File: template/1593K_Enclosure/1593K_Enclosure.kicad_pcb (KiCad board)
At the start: 2 copper layers, 56.6 x 57.7 mm, 1 part

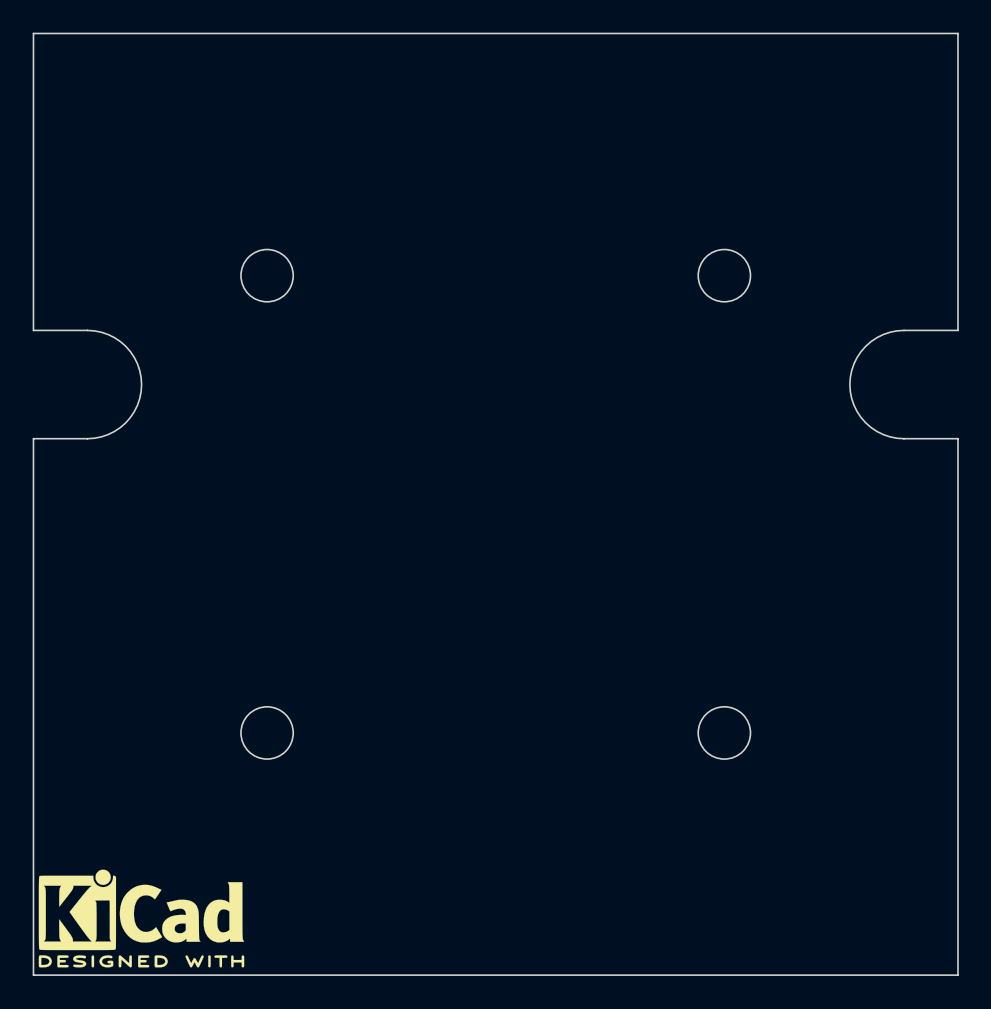
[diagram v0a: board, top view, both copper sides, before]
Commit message: Updated mounting holes from circular edge cuts to actual mounting holes. Added mounting hole symbols to schematic.
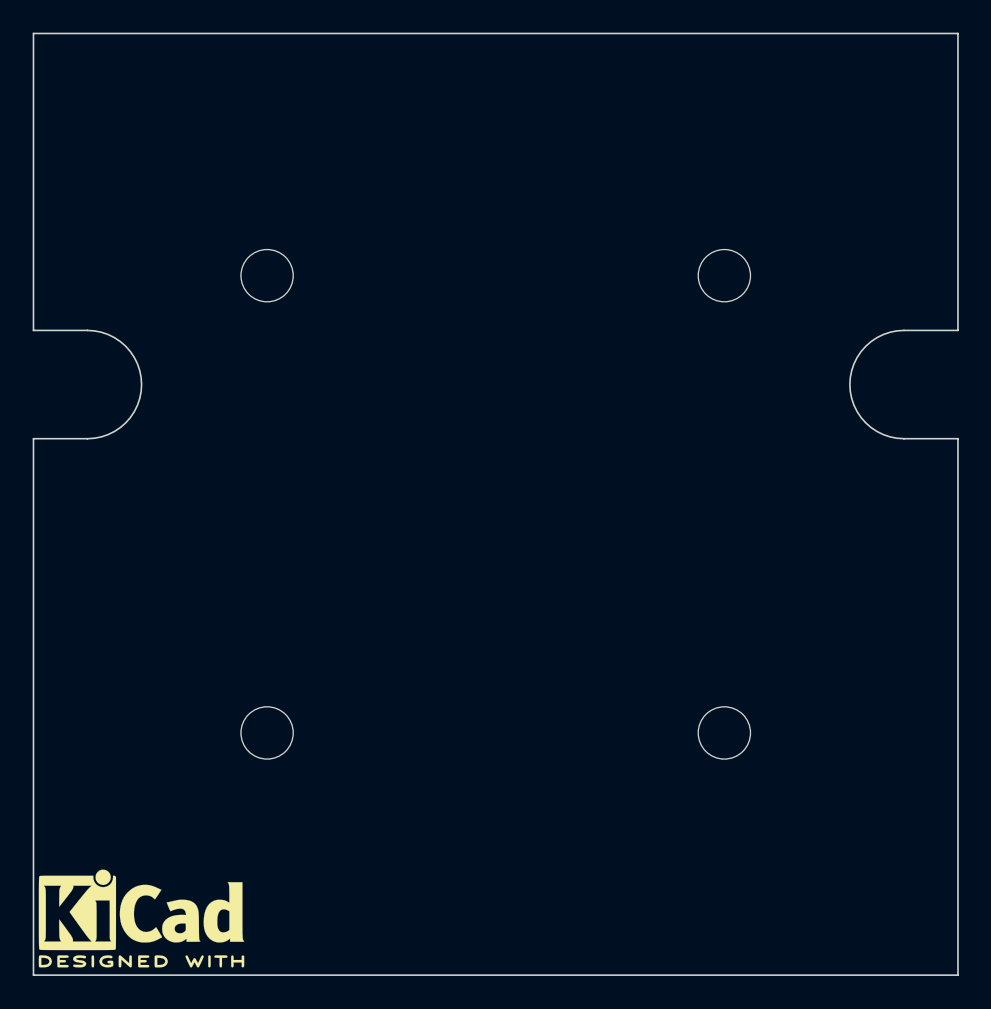
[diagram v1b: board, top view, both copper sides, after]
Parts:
- added MK1: MountingHole_3.2mm_M3_ISO14580, Mounting_Holes:MountingHole_3.2mm_M3_ISO14580, F.Cu at (87.7, 96.6)
- added MK2: MountingHole_3.2mm_M3_ISO14580, Mounting_Holes:MountingHole_3.2mm_M3_ISO14580, F.Cu at (115.7, 96.6)
- added MK3: MountingHole_3.2mm_M3_ISO14580, Mounting_Holes:MountingHole_3.2mm_M3_ISO14580, F.Cu at (87.7, 124.6)
- added MK4: MountingHole_3.2mm_M3_ISO14580, Mounting_Holes:MountingHole_3.2mm_M3_ISO14580, F.Cu at (115.7, 124.6)
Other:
- outline, holes or cut-outs redrawn
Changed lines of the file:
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@@
-(kicad_pcb (version 20160815) (host pcbnew no-vcs-found-undefined)
+(kicad_pcb (version 20160815) (host pcbnew no-vcs-found-7409~56~ubuntu16.10.1)
   (general
     (links 0)
@@
     (area 69.845 81.766999 134.395 145.67)
     (thickness 1.6)
-    (drawings 19)
+    (drawings 15)
     (tracks 0)
     (zones 0)
-    (modules 1)
+    (modules 5)
     (nets 1)
   )
@@
     (mod_text_size 1 1)
     (mod_text_width 0.15)
-    (pad_size 1.524 1.524)
-    (pad_drill 0.762)
+    (pad_size 3.2 3.2)
+    (pad_drill 3.2)
     (pad_to_mask_clearance 0.0762)
     (aux_axis_origin 130 100)
@@
     (diff_pair_width 0.2)
   )
+  (module Mounting_Holes:MountingHole_3.2mm_M3_ISO14580 locked (layer F.Cu)
+    (at 115.695 124.647)
+    (descr "Mounting Hole 3.2mm, no annular, M3, ISO14580")
+    (tags "mounting hole 3.2mm no annular m3 iso14580")
+    (fp_text reference MK4 (at 0 -3.75) (layer F.SilkS) hide
+      (effects (font (size 1 1) (thickness 0.15)))
+    )
+    (fp_text value MountingHole_3.2mm_M3_ISO14580 (at 0 3.75) (layer F.Fab) hide
+      (effects (font (size 1 1) (thickness 0.15)))
+    )
+    (fp_circle (center 0 0) (end 3 0) (layer F.CrtYd) (width 0.05))
+    (fp_circle (center 0 0) (end 2.75 0) (layer Cmts.User) (width 0.15))
+    (pad 1 np_thru_hole circle (at 0 0) (size 3.2 3.2) (drill 3.2) (layers *.Cu *.Mask))
+  )
+  (module Mounting_Holes:MountingHole_3.2mm_M3_ISO14580 locked (layer F.Cu)
+    (at 87.695 124.647)
+    (descr "Mounting Hole 3.2mm, no annular, M3, ISO14580")
+    (tags "mounting hole 3.2mm no annular m3 iso14580")
+    (fp_text reference MK3 (at 0 -3.75) (layer F.SilkS) hide
+      (effects (font (size 1 1) (thickness 0.15)))
+    )
+    (fp_text value MountingHole_3.2mm_M3_ISO14580 (at 0 3.75) (layer F.Fab) hide
+      (effects (font (size 1 1) (thickness 0.15)))
+    )
+    (fp_circle (center 0 0) (end 3 0) (layer F.CrtYd) (width 0.05))
+    (fp_circle (center 0 0) (end 2.75 0) (layer Cmts.User) (width 0.15))
+    (pad 1 np_thru_hole circle (at 0 0) (size 3.2 3.2) (drill 3.2) (layers *.Cu *.Mask))
+  )
+  (module Mounting_Holes:MountingHole_3.2mm_M3_ISO14580 locked (layer F.Cu)
+    (at 115.695 96.647)
+    (descr "Mounting Hole 3.2mm, no annular, M3, ISO14580")
+    (tags "mounting hole 3.2mm no annular m3 iso14580")
+    (fp_text reference MK2 (at 0 -3.75) (layer F.SilkS) hide
+      (effects (font (size 1 1) (thickness 0.15)))
+    )
+    (fp_text value MountingHole_3.2mm_M3_ISO14580 (at 0 3.75) (layer F.Fab) hide
+      (effects (font (size 1 1) (thickness 0.15)))
+    )
+    (fp_circle (center 0 0) (end 3 0) (layer F.CrtYd) (width 0.05))
+    (fp_circle (center 0 0) (end 2.75 0) (layer Cmts.User) (width 0.15))
+    (pad 1 np_thru_hole circle (at 0 0) (size 3.2 3.2) (drill 3.2) (layers *.Cu *.Mask))
+  )
+  (module Mounting_Holes:MountingHole_3.2mm_M3_ISO14580 locked (layer F.Cu)
+    (at 87.695 96.647)
+    (descr "Mounting Hole 3.2mm, no annular, M3, ISO14580")
+    (tags "mounting hole 3.2mm no annular m3 iso14580")
+    (fp_text reference MK1 (at 0 -3.75) (layer F.SilkS) hide
+      (effects (font (size 1 1) (thickness 0.15)))
+    )
+    (fp_text value MountingHole_3.2mm_M3_ISO14580 (at 0 3.75) (layer F.Fab) hide
+      (effects (font (size 1 1) (thickness 0.15)))
+    )
+    (fp_circle (center 0 0) (end 2.75 0) (layer Cmts.User) (width 0.15))
+    (fp_circle (center 0 0) (end 3 0) (layer F.CrtYd) (width 0.05))
+    (pad 1 np_thru_hole circle (at 0 0) (size 3.2 3.2) (drill 3.2) (layers *.Cu *.Mask))
+  )
   (module Symbols:KiCad-Logo2_6mm_SilkScreen (layer F.Cu)
     (at 80 136)
@@
     (tags "Logo KiCad")
     (attr virtual)
-    (fp_text reference REF*** (at 0 -4) (layer F.SilkS) hide
-      (effects (font (size 1 1) (thickness 0.15)))
-    )
-    (fp_text value KiCad-Logo2_6mm_SilkScreen (at 5 -4) (layer F.Fab) hide
+    (fp_text reference REF*** (at -3.95 -3.37) (layer F.SilkS) hide
+      (effects (font (size 1 1) (thickness 0.15)))
+    )
+    (fp_text value KiCad-Logo2_6mm_SilkScreen (at -7.34 4.17) (layer F.Fab) hide
       (effects (font (size 1 1) (thickness 0.15)))
     )
@@
   (gr_arc (start 126.695 103.315) (end 126.695 106.63) (angle 180) (layer Edge.Cuts) (width 0.1))
   (gr_arc (start 76.695 103.315) (end 76.695 100) (angle 180) (layer Edge.Cuts) (width 0.1))
-  (gr_circle (center 87.695 96.647) (end 89.295 96.647) (layer Edge.Cuts) (width 0.1))
-  (gr_circle (center 115.695 124.647) (end 117.295 124.647) (layer Edge.Cuts) (width 0.1))
-  (gr_circle (center 115.695 96.647) (end 117.295 96.647) (layer Edge.Cuts) (width 0.1))
   (gr_line (start 73.39 81.817) (end 73.39 100) (layer Edge.Cuts) (width 0.1))
   (gr_line (start 130 81.817) (end 73.39 81.817) (layer Edge.Cuts) (width 0.1))
@@
   (gr_line (start 76.695 106.63) (end 73.39 106.63) (layer Edge.Cuts) (width 0.1))
   (gr_line (start 130 106.63) (end 126.695 106.63) (layer Edge.Cuts) (width 0.1))
-  (gr_circle (center 87.695 124.647) (end 89.295 124.647) (layer Edge.Cuts) (width 0.1))
   (gr_line (start 73.39 100) (end 76.695 100) (layer Edge.Cuts) (width 0.1))
   (gr_line (start 130 100) (end 130 81.817) (layer Edge.Cuts) (width 0.1))
